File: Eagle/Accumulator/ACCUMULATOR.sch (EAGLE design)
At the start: 12 parts

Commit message: worked on accumulator
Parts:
- added LED0, LED1, LED10, LED11, LED12, LED13, LED14, LED15, LED2, LED3, LED4, LED5, LED6, LED7, LED8, LED9, SC_000, SC_400, SC_800: (no value), led:LED3MM
- added R0, R1, R10, R11, R12, R13, R14, R15, R2, R3, R4, R5, R6, R7, R8, R9, RSC_000, RSC_400, RSC_800: (no value), rcl:R-US_0204/7
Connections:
- new net N$10: RSC_000.2, SC_000.A
- new net N$11: LED0.C, LED1.C, LED10.C, LED11.C, LED12.C, LED13.C, LED14.C, LED15.C, LED2.C, LED3.C, LED4.C, LED5.C, LED6.C, LED7.C, LED8.C, LED9.C
- new net N$14: LED1.A, R1.1
- new net N$16: LED2.A, R2.1
- new net N$18: LED3.A, R3.1
- new net N$19: LED4.A, R4.1
- new net N$2: RSC_800.2, SC_800.A
- new net N$20: LED5.A, R5.1
- new net N$21: LED6.A, R6.1
- new net N$22: LED7.A, R7.1
- new net N$23: LED8.A, R8.1
- new net N$24: LED9.A, R9.1
- new net N$25: LED10.A, R10.1
- new net N$26: LED11.A, R11.1
- new net N$27: LED12.A, R12.1
- new net N$28: LED13.A, R13.1
- new net N$29: LED14.A, R14.1
- new net N$3: RSC_400.2, SC_400.A
- new net N$30: LED15.A, R15.1
- new net N$31: LED0.A, R0.1
- net AC0: now also R0.2
- net AC1: now also R1.2
- net AC10: now also R10.2
- net AC11: now also R11.2
- net AC12: now also R12.2
- net AC13: now also R13.2
- net AC14: now also R14.2
- net AC15: now also R15.2
- net AC2: now also R2.2
- net AC3: now also R3.2
- net AC4: now also R4.2
- net AC5: now also R5.2
- net AC6: now also R6.2
- net AC7: now also R7.2
- net AC8: now also R8.2
- net AC9: now also R9.2
- net GND: now also SC_000.C, SC_400.C, SC_800.C, SKIPCOND.A4, SKIPCOND.A5, SKIPCOND.A6, SKIPCOND.A7, SKIPCOND.A8
- net N$17: now also RSC_800.1
- net N$8: now also RSC_400.1
- net N$9: now also RSC_000.1

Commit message: finished most boards
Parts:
- added C1, C2, C3, C4: (no value), rcl:C-US025-024X044
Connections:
- net GND: now also C1.1, C2.1, C3.1, C4.1
- net VCC: now also C1.2, C2.2, C3.2, C4.2
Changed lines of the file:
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@@
 <part name="R15" library="rcl" library_urn="urn:adsk.eagle:library:334" deviceset="R-US_" device="0204/7" package3d_urn="urn:adsk.eagle:package:23498/2"/>
 <part name="R0" library="rcl" library_urn="urn:adsk.eagle:library:334" deviceset="R-US_" device="0204/7" package3d_urn="urn:adsk.eagle:package:23498/2"/>
+<part name="C1" library="rcl" library_urn="urn:adsk.eagle:library:334" deviceset="C-US" device="025-024X044" package3d_urn="urn:adsk.eagle:package:23630/1"/>
+<part name="C2" library="rcl" library_urn="urn:adsk.eagle:library:334" deviceset="C-US" device="025-024X044" package3d_urn="urn:adsk.eagle:package:23630/1"/>
+<part name="C3" library="rcl" library_urn="urn:adsk.eagle:library:334" deviceset="C-US" device="025-024X044" package3d_urn="urn:adsk.eagle:package:23630/1"/>
+<part name="C4" library="rcl" library_urn="urn:adsk.eagle:library:334" deviceset="C-US" device="025-024X044" package3d_urn="urn:adsk.eagle:package:23630/1"/>
 </parts>
 <sheets>
@@
 <attribute name="VALUE" x="275.082" y="24.13" size="1.778" layer="96" rot="R90"/>
 </instance>
+<instance part="C1" gate="G$1" x="10.16" y="238.76" smashed="yes" rot="R180">
+<attribute name="NAME" x="9.144" y="238.125" size="1.778" layer="95" rot="R180"/>
+<attribute name="VALUE" x="9.144" y="242.951" size="1.778" layer="96" rot="R180"/>
+</instance>
+<instance part="C2" gate="G$1" x="25.4" y="238.76" smashed="yes" rot="R180">
+<attribute name="NAME" x="24.384" y="238.125" size="1.778" layer="95" rot="R180"/>
+<attribute name="VALUE" x="24.384" y="242.951" size="1.778" layer="96" rot="R180"/>
+</instance>
+<instance part="C3" gate="G$1" x="40.64" y="238.76" smashed="yes" rot="R180">
+<attribute name="NAME" x="39.624" y="238.125" size="1.778" layer="95" rot="R180"/>
+<attribute name="VALUE" x="39.624" y="242.951" size="1.778" layer="96" rot="R180"/>
+</instance>
+<instance part="C4" gate="G$1" x="55.88" y="238.76" smashed="yes" rot="R180">
+<attribute name="NAME" x="54.864" y="238.125" size="1.778" layer="95" rot="R180"/>
+<attribute name="VALUE" x="54.864" y="242.951" size="1.778" layer="96" rot="R180"/>
+</instance>
 </instances>
 <busses>
@@
 <wire x1="279.4" y1="83.82" x2="281.94" y2="83.82" width="0.1524" layer="91"/>
 <label x="281.94" y="83.82" size="1.778" layer="95"/>
+</segment>
+<segment>
+<pinref part="C1" gate="G$1" pin="2"/>
+<wire x1="10.16" y1="243.84" x2="10.16" y2="251.46" width="0.1524" layer="91"/>
+<pinref part="C4" gate="G$1" pin="2"/>
+<wire x1="10.16" y1="251.46" x2="25.4" y2="251.46" width="0.1524" layer="91"/>
+<wire x1="25.4" y1="251.46" x2="30.48" y2="251.46" width="0.1524" layer="91"/>
+<wire x1="30.48" y1="251.46" x2="40.64" y2="251.46" width="0.1524" layer="91"/>
+<wire x1="40.64" y1="251.46" x2="55.88" y2="251.46" width="0.1524" layer="91"/>
+<wire x1="55.88" y1="251.46" x2="55.88" y2="243.84" width="0.1524" layer="91"/>
+<pinref part="C3" gate="G$1" pin="2"/>
+<wire x1="40.64" y1="243.84" x2="40.64" y2="251.46" width="0.1524" layer="91"/>
+<junction x="40.64" y="251.46"/>
+<pinref part="C2" gate="G$1" pin="2"/>
+<wire x1="25.4" y1="243.84" x2="25.4" y2="251.46" width="0.1524" layer="91"/>
+<junction x="25.4" y="251.46"/>
+<wire x1="30.48" y1="251.46" x2="30.48" y2="254" width="0.1524" layer="91"/>
+<junction x="30.48" y="251.46"/>
+<label x="30.48" y="254" size="1.778" layer="95" rot="R90"/>
 </segment>
 </net>
@@
 <label x="284.48" y="208.28" size="1.778" layer="95"/>
 </segment>
+<segment>
+<pinref part="C1" gate="G$1" pin="1"/>
+<wire x1="10.16" y1="236.22" x2="10.16" y2="231.14" width="0.1524" layer="91"/>
+<wire x1="10.16" y1="231.14" x2="25.4" y2="231.14" width="0.1524" layer="91"/>
+<pinref part="C4" gate="G$1" pin="1"/>
+<wire x1="25.4" y1="231.14" x2="30.48" y2="231.14" width="0.1524" layer="91"/>
+<wire x1="30.48" y1="231.14" x2="40.64" y2="231.14" width="0.1524" layer="91"/>
+<wire x1="40.64" y1="231.14" x2="55.88" y2="231.14" width="0.1524" layer="91"/>
+<wire x1="55.88" y1="231.14" x2="55.88" y2="236.22" width="0.1524" layer="91"/>
+<pinref part="C3" gate="G$1" pin="1"/>
+<wire x1="40.64" y1="236.22" x2="40.64" y2="231.14" width="0.1524" layer="91"/>
+<junction x="40.64" y="231.14"/>
+<pinref part="C2" gate="G$1" pin="1"/>
+<wire x1="25.4" y1="236.22" x2="25.4" y2="231.14" width="0.1524" layer="91"/>
+<junction x="25.4" y="231.14"/>
+<wire x1="30.48" y1="231.14" x2="30.48" y2="228.6" width="0.1524" layer="91"/>
+<junction x="30.48" y="231.14"/>
+<label x="30.48" y="228.6" size="1.778" layer="95" rot="R270"/>
+</segment>
 </net>

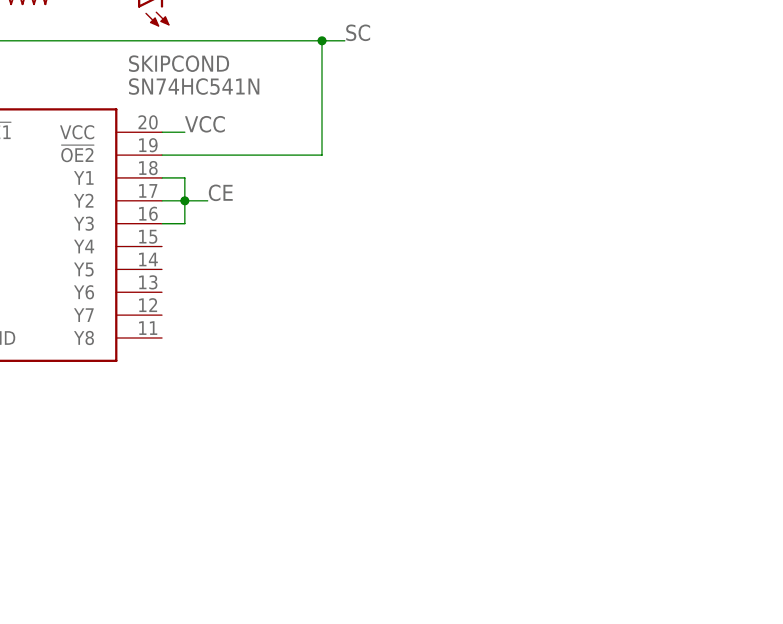
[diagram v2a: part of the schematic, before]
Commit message: added Clock
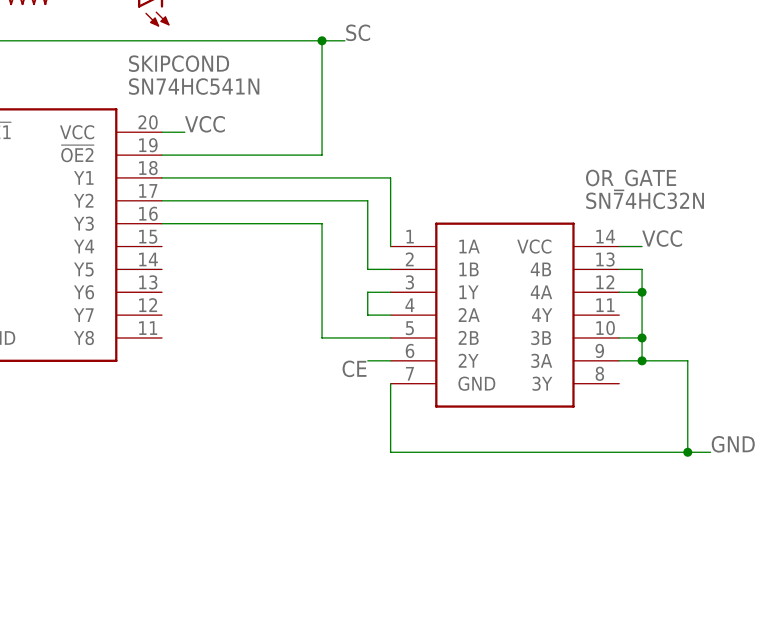
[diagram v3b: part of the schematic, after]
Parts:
- added OR_GATE: SN74HC32N, SamacSys_Parts:SN74HC32N
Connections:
- new net N$32: OR_GATE.1A, SKIPCOND.Y1
- new net N$33: OR_GATE.1B, SKIPCOND.Y2
- new net N$34: OR_GATE.1Y, OR_GATE.2A
- new net N$35: OR_GATE.2B, SKIPCOND.Y3
- net CE: now also OR_GATE.2Y; no longer SKIPCOND.Y1, SKIPCOND.Y2, SKIPCOND.Y3
- net GND: now also OR_GATE.3A, OR_GATE.3B, OR_GATE.4A, OR_GATE.4B, OR_GATE.GND
- net VCC: now also OR_GATE.VCC
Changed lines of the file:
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@@
 <part name="C3" library="rcl" library_urn="urn:adsk.eagle:library:334" deviceset="C-US" device="025-024X044" package3d_urn="urn:adsk.eagle:package:23630/1"/>
 <part name="C4" library="rcl" library_urn="urn:adsk.eagle:library:334" deviceset="C-US" device="025-024X044" package3d_urn="urn:adsk.eagle:package:23630/1"/>
+<part name="OR_GATE" library="SamacSys_Parts" deviceset="SN74HC32N" device=""/>
 </parts>
 <sheets>
@@
 <attribute name="NAME" x="54.864" y="238.125" size="1.778" layer="95" rot="R180"/>
 <attribute name="VALUE" x="54.864" y="242.951" size="1.778" layer="96" rot="R180"/>
+</instance>
+<instance part="OR_GATE" gate="G$1" x="299.72" y="170.18" smashed="yes">
+<attribute name="NAME" x="321.31" y="177.8" size="1.778" layer="95" align="center-left"/>
+<attribute name="VALUE" x="321.31" y="175.26" size="1.778" layer="96" align="center-left"/>
 </instance>
 </instances>
@@
 <junction x="30.48" y="251.46"/>
 <label x="30.48" y="254" size="1.778" layer="95" rot="R90"/>
+</segment>
+<segment>
+<pinref part="OR_GATE" gate="G$1" pin="VCC"/>
+<wire x1="325.12" y1="170.18" x2="327.66" y2="170.18" width="0.1524" layer="91"/>
+<label x="327.66" y="170.18" size="1.778" layer="95"/>
 </segment>
 </net>
@@
 <label x="30.48" y="228.6" size="1.778" layer="95" rot="R270"/>
 </segment>
+<segment>
+<pinref part="OR_GATE" gate="G$1" pin="4B"/>
+<wire x1="325.12" y1="167.64" x2="327.66" y2="167.64" width="0.1524" layer="91"/>
+<wire x1="327.66" y1="167.64" x2="327.66" y2="165.1" width="0.1524" layer="91"/>
+<pinref part="OR_GATE" gate="G$1" pin="4A"/>
+<wire x1="327.66" y1="165.1" x2="325.12" y2="165.1" width="0.1524" layer="91"/>
+<pinref part="OR_GATE" gate="G$1" pin="GND"/>
+<wire x1="299.72" y1="154.94" x2="299.72" y2="147.32" width="0.1524" layer="91"/>
+<wire x1="299.72" y1="147.32" x2="332.74" y2="147.32" width="0.1524" layer="91"/>
+<wire x1="332.74" y1="147.32" x2="332.74" y2="157.48" width="0.1524" layer="91"/>
+<pinref part="OR_GATE" gate="G$1" pin="3A"/>
+<wire x1="332.74" y1="157.48" x2="327.66" y2="157.48" width="0.1524" layer="91"/>
+<pinref part="OR_GATE" gate="G$1" pin="3B"/>
+<wire x1="327.66" y1="157.48" x2="325.12" y2="157.48" width="0.1524" layer="91"/>
+<wire x1="325.12" y1="160.02" x2="327.66" y2="160.02" width="0.1524" layer="91"/>
+<wire x1="327.66" y1="160.02" x2="327.66" y2="157.48" width="0.1524" layer="91"/>
+<junction x="327.66" y="157.48"/>
+<wire x1="327.66" y1="165.1" x2="327.66" y2="160.02" width="0.1524" layer="91"/>
+<junction x="327.66" y="165.1"/>
+<junction x="327.66" y="160.02"/>
+<wire x1="332.74" y1="147.32" x2="335.28" y2="147.32" width="0.1524" layer="91"/>
+<junction x="332.74" y="147.32"/>
+<label x="335.28" y="147.32" size="1.778" layer="95"/>
+</segment>
 </net>
 <net name="N$1" class="0">
@@
 <net name="CE" class="0">
 <segment>
-<pinref part="SKIPCOND" gate="G$1" pin="Y1"/>
-<wire x1="274.32" y1="177.8" x2="276.86" y2="177.8" width="0.1524" layer="91"/>
-<wire x1="276.86" y1="177.8" x2="276.86" y2="175.26" width="0.1524" layer="91"/>
-<pinref part="SKIPCOND" gate="G$1" pin="Y2"/>
-<wire x1="276.86" y1="175.26" x2="274.32" y2="175.26" width="0.1524" layer="91"/>
-<pinref part="SKIPCOND" gate="G$1" pin="Y3"/>
-<wire x1="274.32" y1="172.72" x2="276.86" y2="172.72" width="0.1524" layer="91"/>
-<wire x1="276.86" y1="172.72" x2="276.86" y2="175.26" width="0.1524" layer="91"/>
-<junction x="276.86" y="175.26"/>
-<wire x1="276.86" y1="175.26" x2="279.4" y2="175.26" width="0.1524" layer="91"/>
-<label x="279.4" y="175.26" size="1.778" layer="95"/>
-</segment>
-<segment>
 <pinref part="BUS" gate="G$1" pin="22"/>
 <wire x1="256.54" y1="81.28" x2="254" y2="81.28" width="0.1524" layer="91"/>
 <label x="254" y="81.28" size="1.778" layer="95" rot="R180"/>
+</segment>
+<segment>
+<pinref part="OR_GATE" gate="G$1" pin="2Y"/>
+<wire x1="299.72" y1="157.48" x2="297.18" y2="157.48" width="0.1524" layer="91"/>
+<label x="297.18" y="157.48" size="1.778" layer="95" rot="R180"/>
 </segment>
 </net>
@@
 </segment>
 </net>
+<net name="N$32" class="0">
+<segment>
+<pinref part="SKIPCOND" gate="G$1" pin="Y1"/>
+<wire x1="274.32" y1="177.8" x2="299.72" y2="177.8" width="0.1524" layer="91"/>
+<pinref part="OR_GATE" gate="G$1" pin="1A"/>
+<wire x1="299.72" y1="177.8" x2="299.72" y2="170.18" width="0.1524" layer="91"/>
+</segment>
+</net>
+<net name="N$33" class="0">
+<segment>
+<pinref part="SKIPCOND" gate="G$1" pin="Y2"/>
+<wire x1="274.32" y1="175.26" x2="297.18" y2="175.26" width="0.1524" layer="91"/>
+<wire x1="297.18" y1="175.26" x2="297.18" y2="167.64" width="0.1524" layer="91"/>
+<pinref part="OR_GATE" gate="G$1" pin="1B"/>
+<wire x1="297.18" y1="167.64" x2="299.72" y2="167.64" width="0.1524" layer="91"/>
+</segment>
+</net>
+<net name="N$34" class="0">
+<segment>
+<pinref part="OR_GATE" gate="G$1" pin="1Y"/>
+<wire x1="299.72" y1="165.1" x2="297.18" y2="165.1" width="0.1524" layer="91"/>
+<wire x1="297.18" y1="165.1" x2="297.18" y2="162.56" width="0.1524" layer="91"/>
+<pinref part="OR_GATE" gate="G$1" pin="2A"/>
+<wire x1="297.18" y1="162.56" x2="299.72" y2="162.56" width="0.1524" layer="91"/>
+</segment>
+</net>
+<net name="N$35" class="0">
+<segment>
+<pinref part="SKIPCOND" gate="G$1" pin="Y3"/>
+<wire x1="274.32" y1="172.72" x2="292.1" y2="172.72" width="0.1524" layer="91"/>
+<wire x1="292.1" y1="172.72" x2="292.1" y2="160.02" width="0.1524" layer="91"/>
+<pinref part="OR_GATE" gate="G$1" pin="2B"/>
+<wire x1="292.1" y1="160.02" x2="299.72" y2="160.02" width="0.1524" layer="91"/>
+</segment>
+</net>

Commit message: started adding revision 2 to fix errors in first set of boards
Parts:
- LED0, LED1, LED10, LED11, LED12, LED13, LED14, LED15, LED2, LED3, LED4, LED5, LED6, LED7, LED8, LED9: value (none) -> RED
- R0, R1, R10, R11, R12, R13, R14, R15, R2, R3, R4, R5, R6, R7, R8, R9, RSC_000, RSC_400, RSC_800: value (none) -> 220
- SC_000, SC_400, SC_800: value (none) -> YELLOW
